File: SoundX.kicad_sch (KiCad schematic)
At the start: 55 parts, among them CN1 EDGE_CONN, CN2 AUDIO_OUT, CN3 CONN_MIDI_IN, CN4 CONN_MIDI_OUT, U1 GAL20V8, U2 MC6850, U3 YM3526, U4 6N138, U5 74HCT74, U6 YM3014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

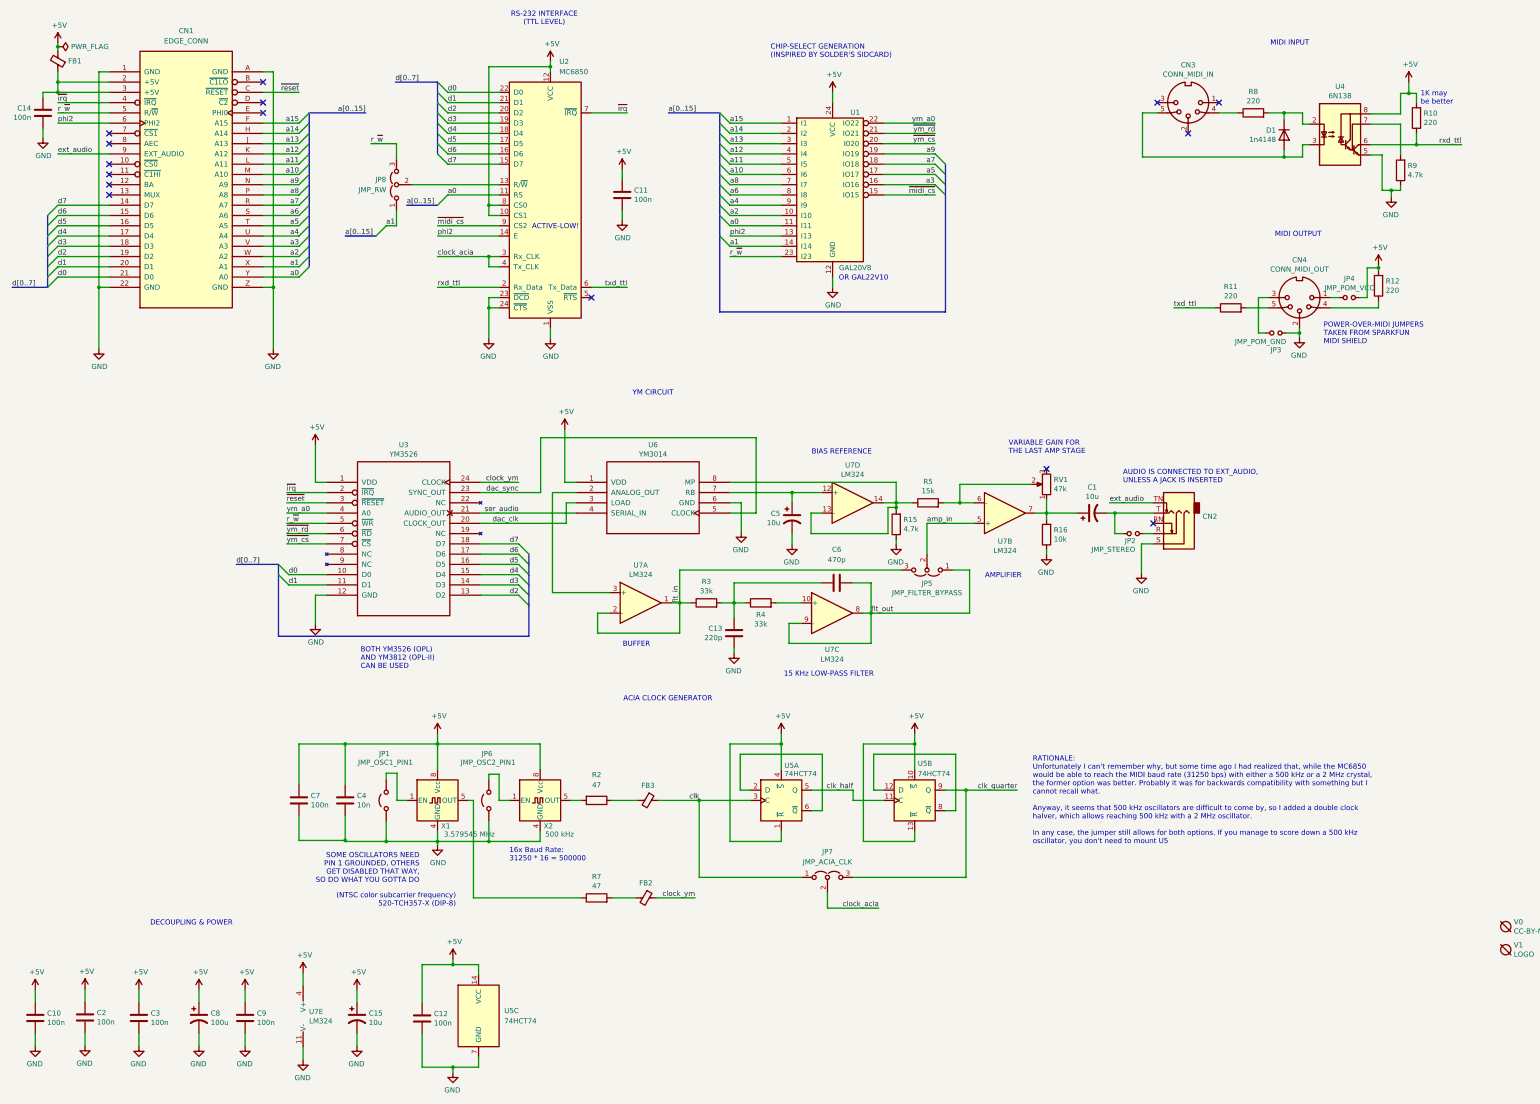
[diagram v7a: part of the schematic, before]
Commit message: Better edge connector
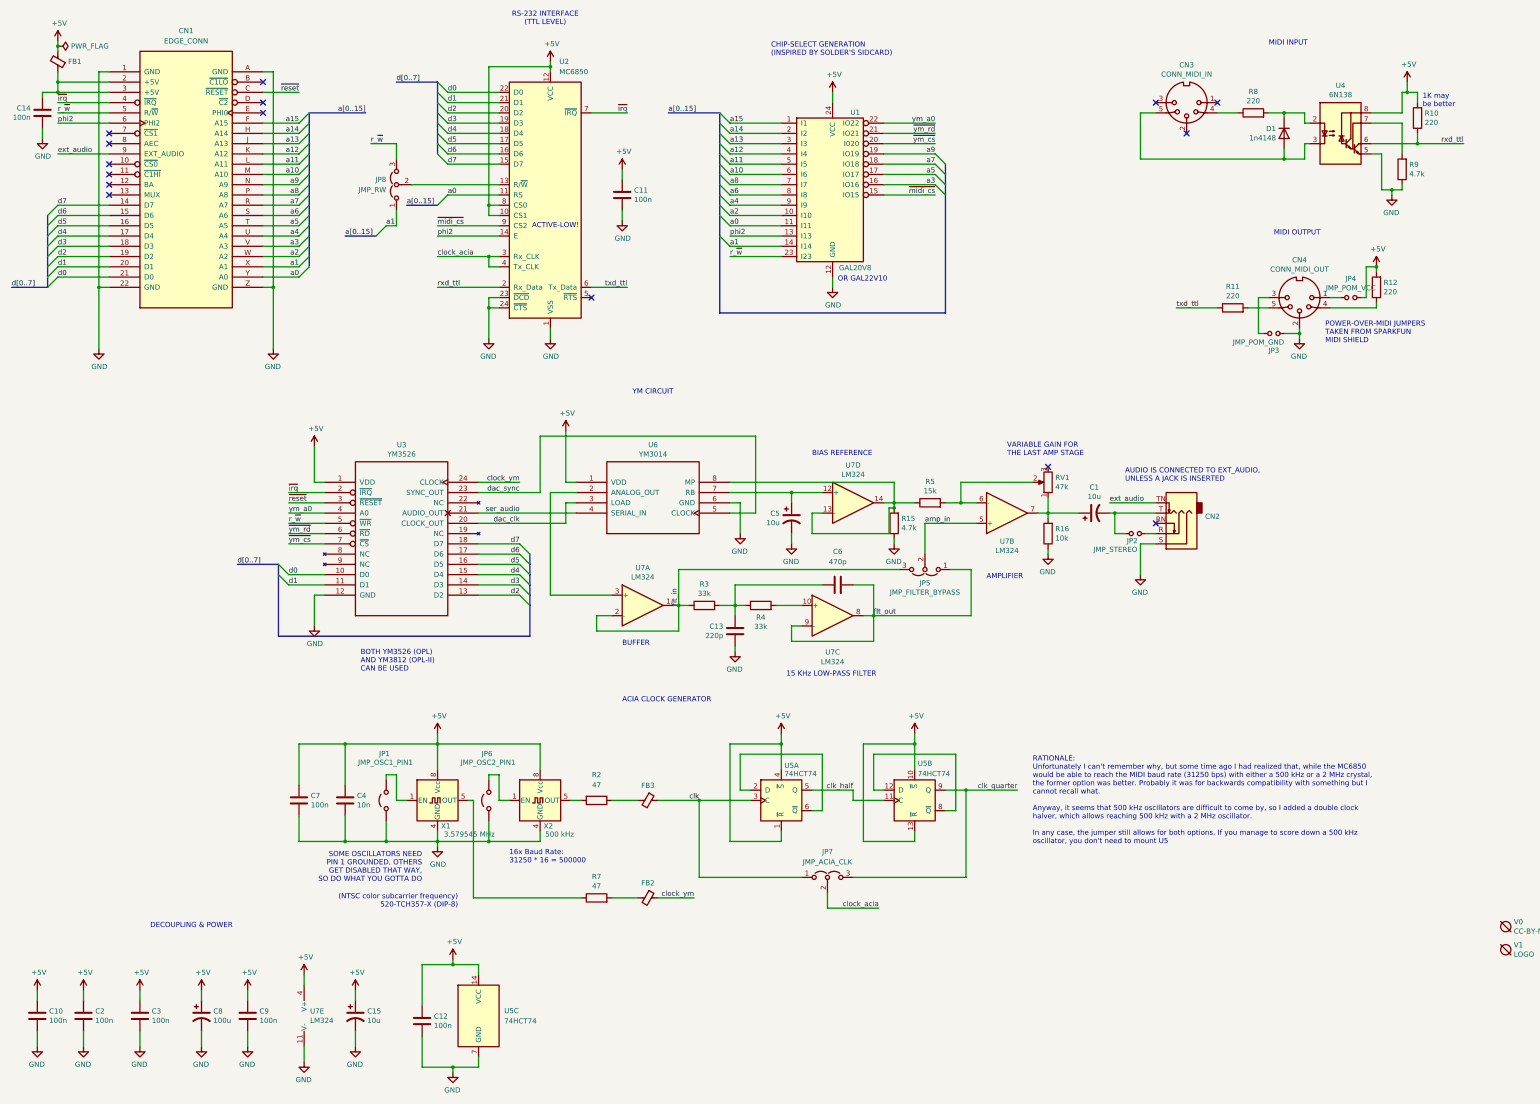
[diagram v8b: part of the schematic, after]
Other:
- moved on the sheet: C1, C10, C12, C13, C15, C2, C3, C6, C8, C9, CN2, FB2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
